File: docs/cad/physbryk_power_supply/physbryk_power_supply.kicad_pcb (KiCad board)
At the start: 2 copper layers, 50.8 x 72.4 mm, 11 parts, among them U1 LM317_TO-220

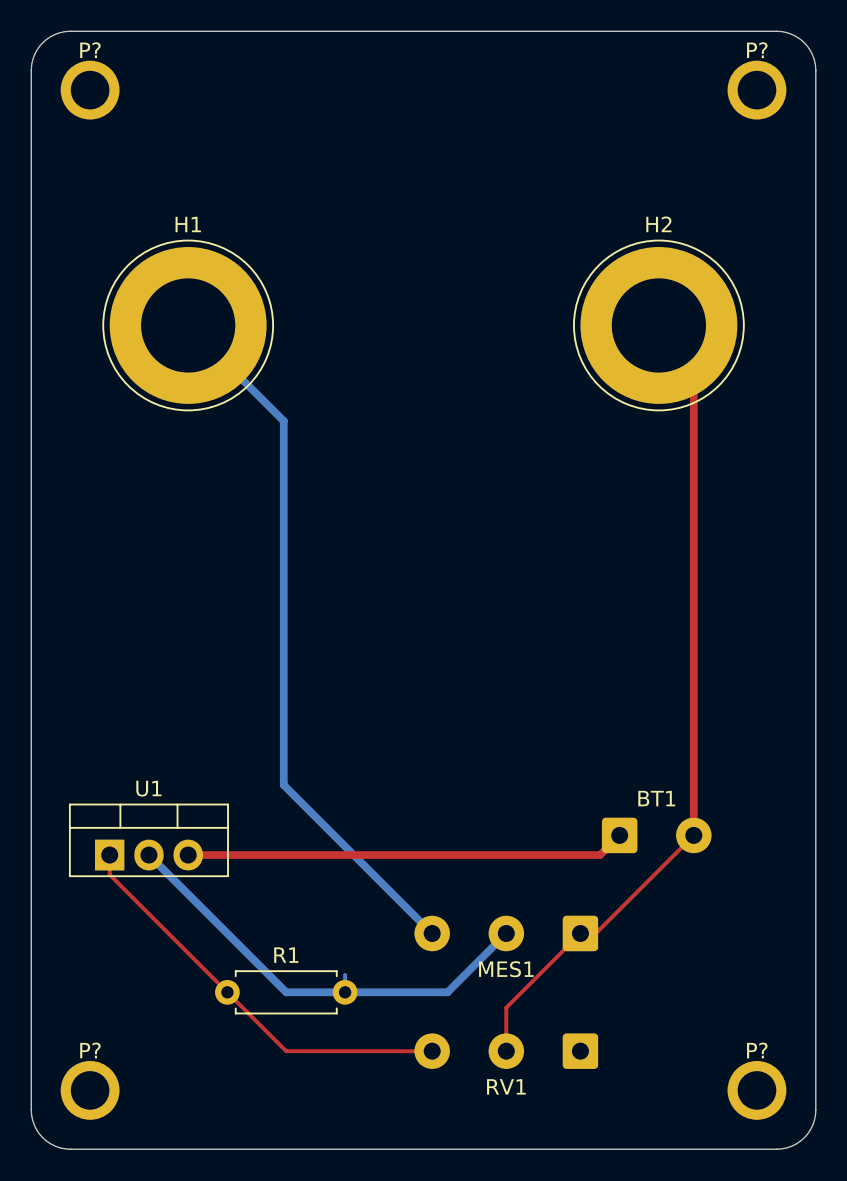
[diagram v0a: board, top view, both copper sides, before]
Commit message: reduced size of power supply pcb
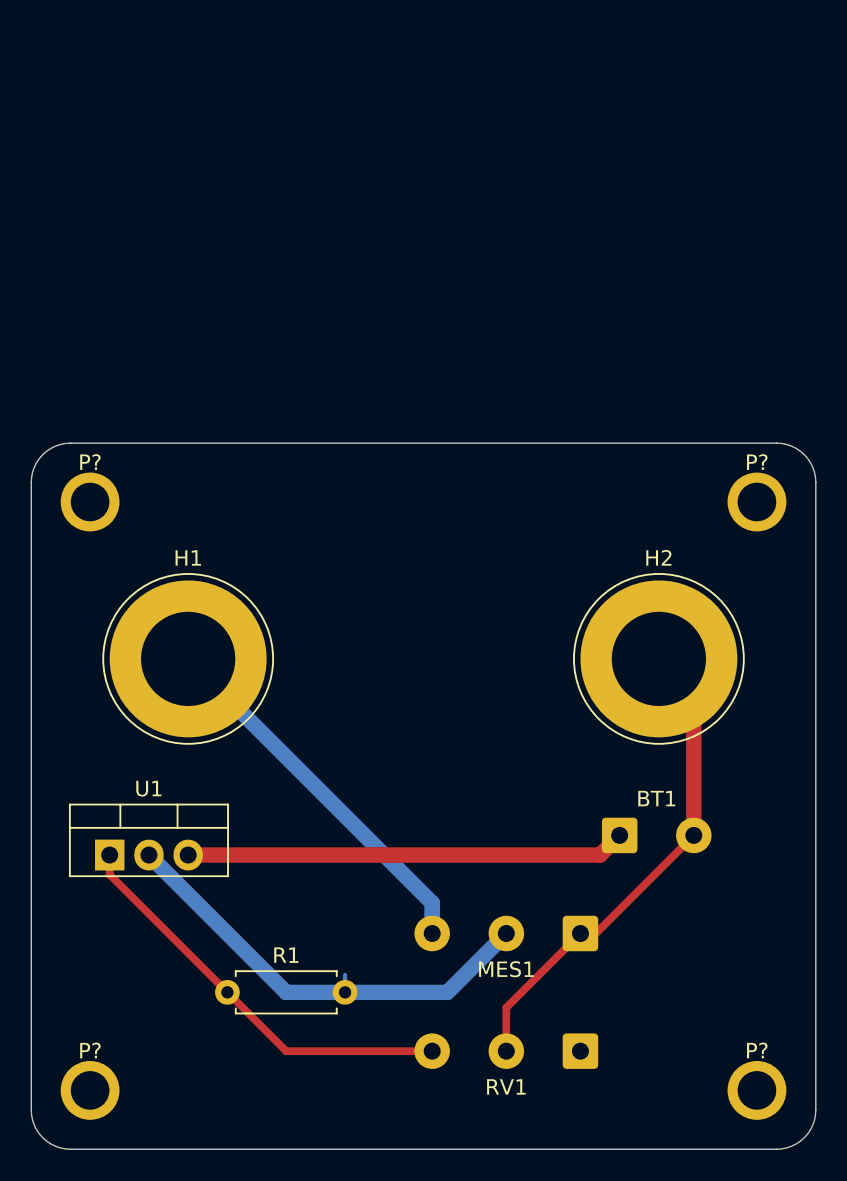
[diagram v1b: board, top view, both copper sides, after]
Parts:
- moved P? 26.7 mm to (171.4, 76.2)
- moved P? 26.7 mm to (128.3, 76.2)
- moved H1 21.6 mm to (134.6, 86.4)
- moved H2 21.6 mm to (165.1, 86.4)
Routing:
- net GND: track 54.5 -> 31.9 mm
- net Net-(H1-Pad1): track 45.9 -> 24.3 mm
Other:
- board size 50.8 x 72.4 mm -> 50.8 x 45.7 mm
